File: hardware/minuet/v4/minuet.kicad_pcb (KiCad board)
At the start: 2 copper layers, 79 x 79 mm, 88 parts, among them J1 B2P-VH-B, J10 G800LE300018YEU, J11 MTJ-889X1, J12 MTJ-669X1, J2 B2B-XH-A, J3 B2B-XH-A, J4 PPPC082LFBN-RC, J5 B2B-XH-A, J6 USB4105-GF-A, J7 SM04B-SRSS-TB, J8 B3P-VH-B, J9 B2B-XH-A, Q1 MMBT3904, SW1 EVQ-P7A01P, SW2 EVQ-P7A01P, U1 TSOP39238, U2 LMV331IDCK, U3 TCA9555RTW, U4 ESP32-C3-WROOM-02-N4, U5 MCF8316D, U6 DRV8876PWP

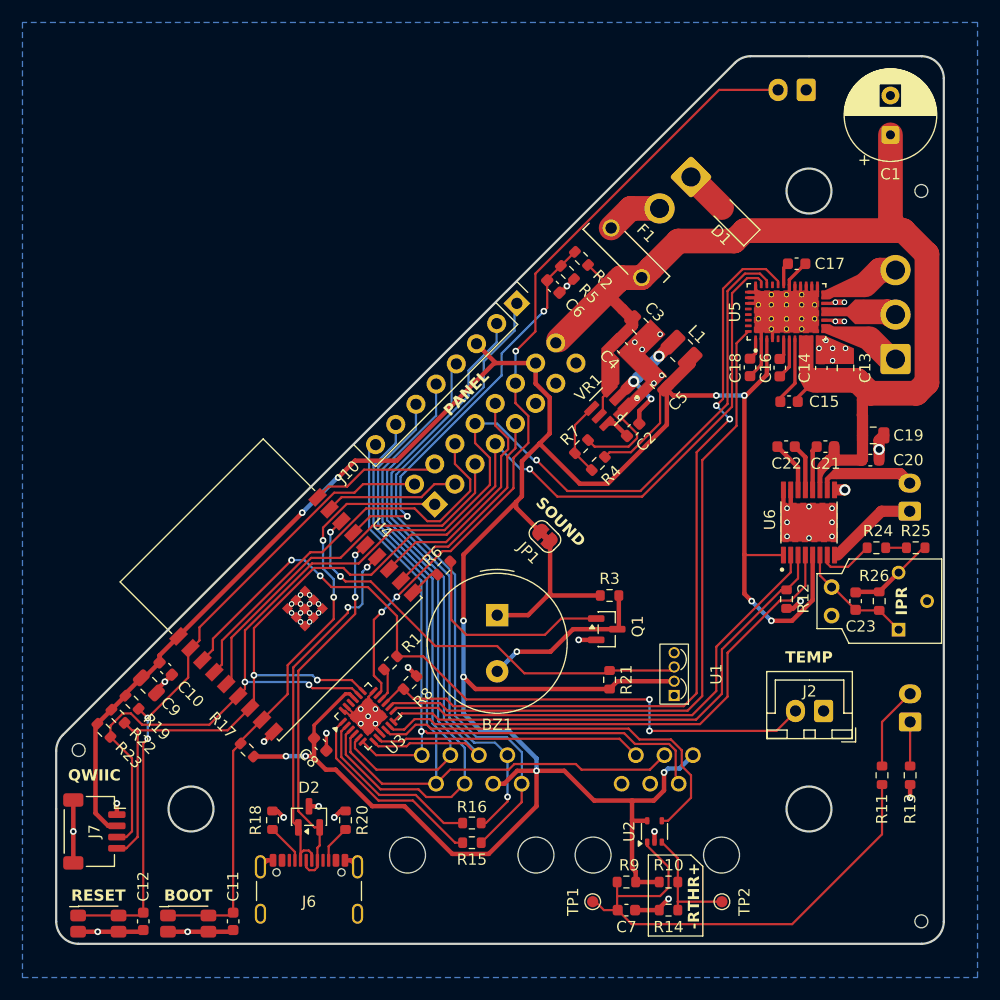
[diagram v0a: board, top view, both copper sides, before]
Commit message: First draft of Minuet v4 fan controller board
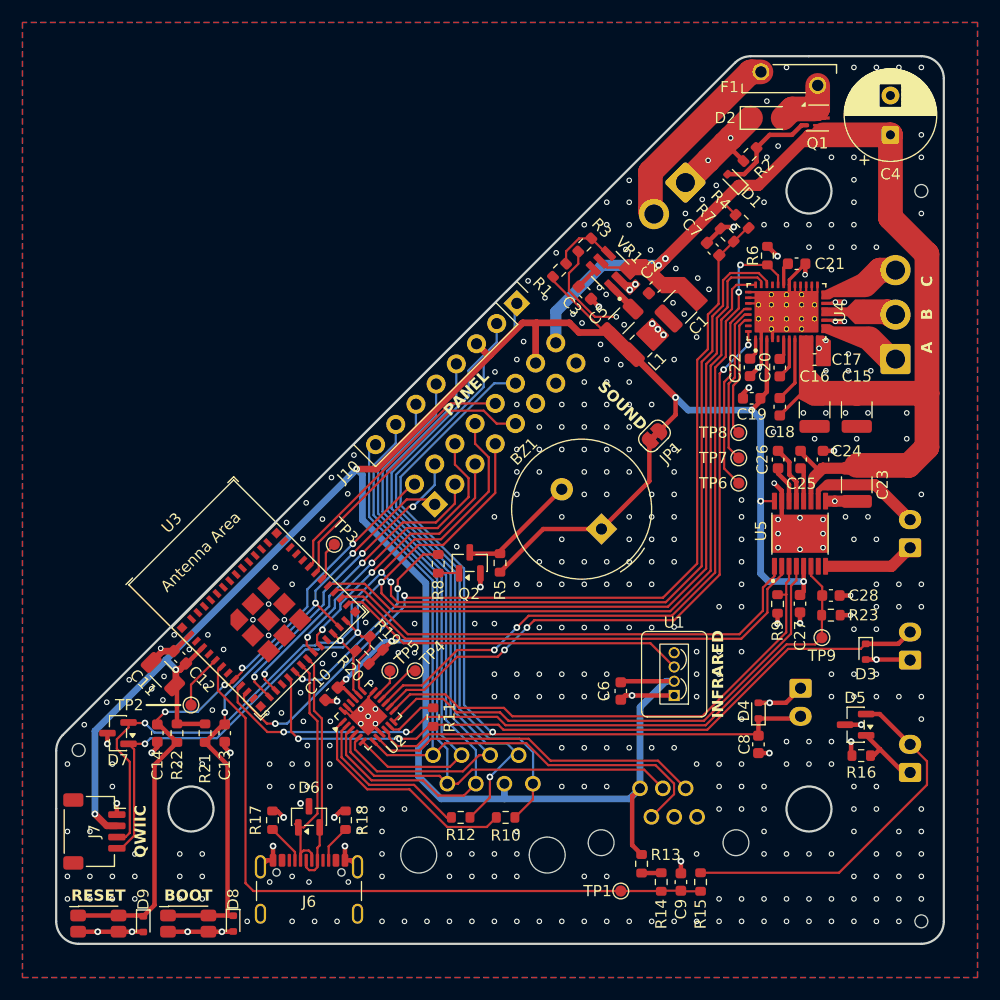
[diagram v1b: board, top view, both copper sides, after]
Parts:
- removed the C13 at (103.2, 60.8)
- removed the C3 at (85.0, 57.0)
- removed the C9 at (41.2, 89.0)
- removed the NT3 at (61.5, 88.4)
- removed NT4: NetTie_2, Generic:NetTie-2_SMD_Pad1.0mm
- removed the R10 at (87.5, 106.5)
- removed the R14 at (87.5, 109.0)
- removed the R21 at (82.2, 88.5)
- removed R24: 51K, Resistor_SMD:R_0603_1608Metric
- removed R25: 10K, Resistor_SMD:R_0603_1608Metric
- removed RV1: 5K, 3362P-1-502LF:TRIM_3362P-1-502LF
- removed the U2 at (86.2, 102.0)
- removed the U4 at (54.2, 82.6)
- added C1: 10u, Capacitor_SMD:C_1210_3225Metric, F.Cu at (88.5, 55.3)
- added C11: 47u, Capacitor_SMD:C_1206_3216Metric, F.Cu at (42.5, 88.0)
- added C15: 10u, Capacitor_SMD:C_1210_3225Metric, F.Cu at (104.2, 64.5)
- added C16: 10u, Capacitor_SMD:C_1210_3225Metric, F.Cu at (100.5, 64.5)
- added C23: 10u, Capacitor_SMD:C_1210_3225Metric, F.Cu at (104.2, 71.2)
- added C27: 100n, Capacitor_SMD:C_0603_1608Metric, F.Cu at (99.2, 81.7)
- added C6: 100n, Capacitor_SMD:C_0603_1608Metric, F.Cu at (83.2, 89.5)
- added C8: 100n, Capacitor_SMD:C_0603_1608Metric, F.Cu at (95.5, 94.2)
- added D2: SMF16CA, Diode_SMD:D_SMF, F.Cu at (96.2, 38.5)
- added D3: PESD5Z3.3, Diode_SMD:D_SOD-523, F.Cu at (105.0, 86.0)
- added D4: PESD5Z3.3, Diode_SMD:D_SOD-523, F.Cu at (95.5, 91.2)
- added D5: PESD3V3S2UT, Package_TO_SOT_SMD:SOT-23, F.Cu at (104.2, 92.5)
- added D7: PESD3V3S2UT, Package_TO_SOT_SMD:SOT-23, F.Cu at (38.5, 93.2)
- added D8: PESD5Z3.3, Diode_SMD:D_SOD-523, F.Cu at (48.8, 110.2)
- added D9: PESD5Z3.3, Diode_SMD:D_SOD-523, F.Cu at (40.8, 110.2)
- added NT1: NetTie_2, Generic:NetTie-2_SMD_Pad0.2mm, F.Cu at (81.3, 57.0)
- added Q1: SiA445EDJ, Package_TO_SOT_SMD:Vishay_PowerPAK_SC70-6L_Single, F.Cu at (100.8, 38.5)
- added R13: 100K, Resistor_SMD:R_0603_1608Metric, F.Cu at (85.1, 104.9)
- added R2: 100K, Resistor_SMD:R_0603_1608Metric, F.Cu at (94.8, 41.8)
- added TP4: TestPoint_Alt, TestPoint:TestPoint_Pad_D1.0mm, F.Cu at (65.0, 87.7)
- added TP5: TestPoint_Alt, TestPoint:TestPoint_Pad_D1.0mm, F.Cu at (62.7, 87.7)
- added TP6: TestPoint_Alt, TestPoint:TestPoint_Pad_D1.0mm, F.Cu at (93.8, 71.0)
- added TP7: TestPoint_Alt, TestPoint:TestPoint_Pad_D1.0mm, F.Cu at (93.8, 68.8)
- added TP8: TestPoint_Alt, TestPoint:TestPoint_Pad_D1.0mm, F.Cu at (93.8, 66.5)
- added TP9: TestPoint_Alt, TestPoint:TestPoint_Pad_D1.0mm, F.Cu at (101.2, 84.8)
- added U3: ESP32-C6-MINI-1/U, PCM_Espressif:ESP32-C6-MINI-1, F.Cu at (50.0, 81.2)
- C13: renamed from C11; value 10p -> 100n
- C19: value 2.2u -> 1u; footprint Capacitor_SMD:C_0805_2012Metric -> Capacitor_SMD:C_0603_1608Metric
- C5: footprint Capacitor_SMD:C_0805_2012Metric -> Capacitor_SMD:C_1206_3216Metric
- D1: value SMF16A -> BZT52C8V2T; footprint Diode_SMD:D_SMF -> Diode_SMD:D_SOD-523
- J11: footprint MTJ-889X1:CONN_MTJ-889X1_ADM -> MTJ-889X1:MTJ-889X1
- J12: value MTJ-669X1 -> MTJ-662BX2; footprint MTJ-669X1:CONN_MTJ-669X1_ADM -> MTJ-662BX2:MTJ-662BX2
- J2: moved to B.Cu
- NT2: footprint Generic:NetTie-2_SMD_Pad1.0mm -> Generic:NetTie-2_SMD_Pad0.2mm
- R19: renamed from R22; value 10K -> 5.1K
- R20: renamed from R23; value 10K -> 5.1K
- R23: renamed from R26; value 2.21K -> 3.3K
- TP1, TP2: value TestPoint_Small -> TestPoint_Alt
- TP3: value TestPoint_2Pole -> TestPoint_Alt; footprint TestPoint:TestPoint_2Pads_Pitch2.54mm_Drill0.8mm -> TestPoint:TestPoint_Pad_D1.0mm; moved to F.Cu
- moved J3 53.3 mm to (99.2, 89.2), turned to -90 degrees
- moved TP2 50.4 mm to (45.0, 90.8), turned to -135 degrees
- moved R6 49.6 mm to (96.3, 50.8), turned to -90 degrees
- moved TP3 44.7 mm to (57.8, 76.5), turned to 0 degrees
- moved R19 23.9 mm to (61.5, 85.2), turned to -45 degrees
- moved R20 23.9 mm to (60.2, 86.5), turned to -45 degrees
- moved F1 21.2 mm to (98.2, 35.0), turned to 0 degrees
- moved R15 18.7 mm to (90.3, 106.5)
- moved R3 18.0 mm to (80.0, 49.8), turned to 45 degrees
- moved R1 17.5 mm to (77.8, 52.0), turned to -135 degrees
- moved C14 16.8 mm to (42.0, 93.2)
- moved C13 16.8 mm to (48.0, 93.2)
- moved R4 14.7 mm to (94.0, 47.7), turned to 135 degrees
- moved C7 14.6 mm to (91.5, 50.2), turned to 135 degrees
- moved R7 14.6 mm to (92.7, 48.9), turned to -45 degrees
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- renumbered C8 to C10, C10 to C12, C12 to C14, C14 to C17, C15 to C18, C4 to C2, C16 to C20, C17 to C21, C18 to C22, C20 to C24, C21 to C25, C22 to C26, C23 to C28, C2 to C3, C1 to C4, C6 to C7, C7 to C9, D2 to D6, J5 to J3, J3 to J4, J4 to J5, NT1 to NT3, Q1 to Q2, R4 to R1, R15 to R10, R1 to R11, R16 to R12, R9 to R14, R11 to R15, R13 to R16, R18 to R17, R20 to R18, R17 to R21, R19 to R22, R7 to R3, R2 to R4, R3 to R5, R8 to R6, R5 to R7, R6 to R8, R12 to R9, U3 to U2, U5 to U4, U6 to U5
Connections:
- net Net-(J3-Pin_1) renamed /RAIN-
- net Net-(J3-Pin_2) renamed /RAIN+
- net SCL renamed I2C_SCL
- net SDA renamed I2C_SDA
- C19 pad 1: GND -> +3.3V
- C19 pad 2: /lid/VM -> GND
- C2 pad 1: /VIN -> +12V
- C24 pad 1: /lid/VM -> +12V
- C25 pad 1: /lid/VM -> +12V
- C28 pad 1: /lid/IPROPI -> GPIO4
- C7 pad 1: GPIO3 -> GPIO5
- C9 pad 1: /RSEN -> GPIO3
- D1 pad 2: GND -> Net-(D1-A)
- F1 pad 2: +12V -> Net-(D2-A2)
- J10 pad 4: XIO6 -> XIO4
- J10 pad 6: XIO4 -> XIO5
- J10 pad 8: XIO5 -> XIO6
- J11 pad 4: XIO6 -> XIO4
- J11 pad 6: XIO4 -> XIO5
- J11 pad 8: XIO5 -> XIO6
- J12 pad 2: XIO5 -> XIO6
- J2 pad 2: GPIO4 -> GPIO6
- J3 pad 2: LOCK -> XIO8
- J5 pad 12: LOCK -> XIO8
- J5 pad 5: GPIO6 -> GPIO15
- J5 pad 6: GPIO5 -> GPIO14
- NT2 pad 1: +12V -> GND
- NT2 pad 2: /VIN -> Net-(NT2-Pad2)
- R1 pad 2: +3.3V -> Net-(NT1-Pad1)
- R11 pad 1: GPIO4 -> GPIO6
- R11 pad 2: XIO14 -> XIO9
- R14 pad 1: +3.3V -> Net-(R13-Pad1)
- R14 pad 2: /RSEN -> GPIO3
- R15 pad 2: /RSEN -> GPIO3
- R23 pad 1: /lid/IPROPI -> GPIO4
- R3 pad 1: GND -> Net-(NT2-Pad2)
- R4 pad 1: GPIO3 -> GPIO5
- R7 pad 2: GPIO3 -> GPIO5
- R8 pad 2: GPIO10 -> GPIO7
- R9 pad 2: XIO10 -> XIO11
- TP1 pad 1: /RSEN -> GPIO3
- TP2 pad 1: /RTHR -> GPIO2
- TP3 pad 1: GND -> GPIO23
- U1 pad 3: GPIO2_STRAP -> GPIO19
- U4 pad 32: GND -> GPIO22
- U4 pad 36: unconnected-(U5-DACOUT1-Pad36) -> Net-(U4-DACOUT1)
- U4 pad 37: unconnected-(U5-DACOUT2-Pad37) -> Net-(U4-DACOUT2)
- U4 pad 38: unconnected-(U5-DACOUT2/SOX-Pad38) -> Net-(U4-DACOUT2/SOX)
- U5 pad 1: +3.3V -> GPIO21
- U5 pad 11: /lid/VM -> +12V
- U5 pad 16: GND -> +3.3V
- U5 pad 2: XIO11 -> GPIO20
- U5 pad 3: XIO10 -> XIO11
- U5 pad 4: XIO9 -> XIO10
- U5 pad 6: /lid/IPROPI -> GPIO4
- U5 pad 7: /lid/IMODE -> unconnected-(U5-IMODE-Pad7)
- VR1 pad 3: /VIN -> +12V
- VR1 pad 5: /VIN -> +12V
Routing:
- net LOCK: track 71.6 -> 0.00 mm, vias 3 -> 0
- net GPIO22: track 0.00 -> 64.5 mm
- net +3.3V: track 283.8 -> 225.4 mm, vias 12 -> 9
- net /RSEN: track 46.2 -> 0.00 mm
- net GPIO20: track 0.00 -> 45.0 mm
- net GPIO21: track 0.00 -> 44.8 mm
- net GPIO5: track 36.4 -> 80.4 mm, vias 0 -> 2
- net XIO8: track 35.8 -> 79.4 mm, vias 0 -> 1
- net XIO9: track 47.9 -> 4.82 mm
- net GPIO2_STRAP: track 38.9 -> 0.00 mm, vias 2 -> 0
- net GPIO19: track 0.00 -> 31.6 mm
- net GPIO6: track 33.9 -> 64.3 mm, vias 0 -> 2
- net +12V: track 70.2 -> 98.5 mm, vias 0 -> 2
- net GPIO14: track 0.00 -> 26.9 mm, vias 0 -> 2
- net GPIO3: track 35.6 -> 61.0 mm, vias 2 -> 0
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- added copper zone on In1.Cu, net GND
- added copper zone on In2.Cu, net GND
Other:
- copper layers 2 -> 4
- board text added: "12V 3V3 LOCK TXD SDA GPIO14 GPIO0 RESET"
- board text added: "A B C"
- board text added: "Back Pillar"
- board text added: "ESP32-C6"
- board text added: "GND GND (NC) RXD SCL GPIO15 GPIO1 BOOT"
- board text added: "INFRARED"
- board text removed: "-RTHR+"
- board text removed: "12V 3V3 LOCK TXD SDA GPIO5 GPIO0 RESET"
- board text removed: "ESP32-C3"
- board text removed: "GND GND (NC) RXD SCL GPIO6 GPIO1 BOOT"
- board text removed: "IPR"
- board text removed: "LID MOTOR CURRENT LIMIT"

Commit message: Second draft of Minuet v4 main board.
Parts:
- removed the TP2 at (45.0, 90.8)
- added C9: 100n, Capacitor_SMD:C_0603_1608Metric, F.Cu at (79.8, 64.5)
- added R13: 100K, Resistor_SMD:R_0603_1608Metric, F.Cu at (82.0, 62.2)
- R20: renamed from R19; value 5.1K -> 3.3K
- R21: renamed from R20; value 5.1K -> 3.3K
- renumbered C9 to C10, C10 to C11, C11 to C12, C12 to C13, C13 to C14, C14 to C15, C15 to C16, C16 to C17, C17 to C18, C18 to C19, C19 to C20, C20 to C21, C21 to C22, C22 to C23, C23 to C24, C24 to C25, C25 to C26, C26 to C27, C27 to C28, C28 to C29, R13 to R14, R14 to R15, R15 to R16, R16 to R17, R17 to R18, R18 to R19, R21 to R22, R22 to R23, R23 to R24, TP3 to TP2, TP4 to TP3, TP5 to TP4, TP6 to TP5, TP7 to TP6, TP8 to TP7, TP9 to TP8
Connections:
- C10 pad 1: GPIO3 -> GPIO2
- D3 pad 1: GPIO6 -> GPIO3
- J2 pad 2: GPIO6 -> GPIO3
- J5 pad 11: unconnected-(J5-Pin_11-Pad11) -> GPIO6
- R11 pad 1: GPIO6 -> GPIO3
- R15 pad 2: GPIO3 -> GPIO2
- R16 pad 2: GPIO3 -> GPIO2
- TP1 pad 1: GPIO3 -> GPIO2
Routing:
- net GPIO2: track 4.88 -> 61.8 mm
- net GPIO6: track 64.3 -> 43.5 mm
- net GPIO3: track 61.0 -> 69.6 mm, vias 0 -> 2
- net +3.3V: track 225.4 -> 227.8 mm
- net GND: track 95.3 -> 96.4 mm, vias 421 -> 436
- net I2C_SDA: track 130.6 -> 130.3 mm, vias 4 -> 3
- net I2C_SCL: track 127.5 -> 127.3 mm, vias 3 -> 4
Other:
- board text added: "GND GND ID RXD SCL GPIO15 GPIO1 BOOT"
- board text removed: "GND GND (NC) RXD SCL GPIO15 GPIO1 BOOT"

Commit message: Move IR receiver to center on aperture
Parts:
- moved U1 0.71 mm to (87.5, 89.4)
- moved C6 0.60 mm to (83.2, 88.9)
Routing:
- net GPIO19: track 31.6 -> 30.9 mm
- net GND: track 96.4 -> 95.9 mm

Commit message: Prepare main board for fabrication
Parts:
- added TP5: TestPoint_Alt, TestPoint:TestPoint_Pad_D1.0mm, F.Cu at (93.8, 73.2)
- moved C6 1.25 mm to (82.0, 88.9)
- renumbered TP5 to TP6, TP6 to TP7, TP7 to TP8, TP8 to TP9
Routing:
- net +3.3V: track 227.6 -> 228.9 mm
- net GND: track 95.9 -> 97.1 mm
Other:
- board text added: "+ -"
- board text added: "I2C"
- board text removed: "QWIIC"
